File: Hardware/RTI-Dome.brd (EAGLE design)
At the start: 80 x 71.1 mm, 43 parts, among them IC1 24AA128ST, IC2 74LVC244, IC3 FT232RL, X13 PN61729-S

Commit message: Remove I2C 2 pin header as we now have the eeprom on the board.
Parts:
- removed JP4: (no value), jumper:JP1
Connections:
- net SCL: no longer JP4.1
- net SDA: no longer JP4.2
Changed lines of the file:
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@@
 <element name="C1" library="rti" package="C0805" value="10uF" x="30.734" y="54.61" rot="R90"/>
 <element name="R5" library="rti" package="R0805" value="100" x="33.02" y="54.61" rot="R90"/>
-<element name="JP4" library="jumper" package="JP1" value="" x="9.271" y="54.356" rot="R270"/>
 <element name="U$4" library="rti" package="LOGO_BIG" value="RTI-LOGO_BIG" x="3.175" y="18.542"/>
 <element name="C2" library="rti" package="UD-10X10_NICHICON" value="100uF" x="64.77" y="13.97" rot="R270"/>
@@
 </signal>
 <signal name="SDA">
-<contactref element="JP4" pad="2"/>
-<wire x1="10.541" y1="59.3725" x2="10.541" y2="54.356" width="0.4064" layer="1"/>
 <contactref element="PCB1" pad="SDA1"/>
 <contactref element="IC1" pad="5"/>
 <contactref element="R1" pad="1"/>
-<wire x1="10.541" y1="54.356" x2="10.541" y2="51.181" width="0.3048" layer="1"/>
 <wire x1="10.541" y1="51.181" x2="10.16" y2="50.8" width="0.3048" layer="1"/>
 <wire x1="6.055" y1="44.835" x2="6.055" y2="50.505" width="0.3048" layer="1"/>
@@
 <wire x1="7.96925" y1="44.13" x2="7.26425" y2="44.835" width="0.3048" layer="1"/>
 <wire x1="7.26425" y1="44.835" x2="6.055" y2="44.835" width="0.3048" layer="1"/>
+<wire x1="10.541" y1="59.3725" x2="10.541" y2="51.181" width="0.254" layer="1"/>
 </signal>
 <signal name="3.3V">
@@
 <contactref element="IC1" pad="6"/>
 <contactref element="R3" pad="1"/>
-<contactref element="JP4" pad="1"/>
-<wire x1="8.001" y1="59.3725" x2="8.001" y2="54.356" width="0.4064" layer="1"/>
 <contactref element="PCB1" pad="SCL1"/>
 <wire x1="5.405" y1="44.835" x2="5.405" y2="46.101" width="0.3048" layer="1"/>
@@
 <wire x1="6.35" y1="52.07" x2="7.62" y2="52.07" width="0.3048" layer="1"/>
 <wire x1="7.62" y1="52.07" x2="8.001" y2="52.451" width="0.3048" layer="1"/>
-<wire x1="8.001" y1="52.451" x2="8.001" y2="54.356" width="0.3048" layer="1"/>
 <wire x1="2.3495" y1="44.35225" x2="2.54" y2="44.54275" width="0.3048" layer="1"/>
 <wire x1="2.54" y1="44.54275" x2="2.54" y2="45.72" width="0.3048" layer="1"/>
 <wire x1="2.54" y1="45.72" x2="2.921" y2="46.101" width="0.3048" layer="1"/>
 <wire x1="2.921" y1="46.101" x2="5.405" y2="46.101" width="0.3048" layer="1"/>
+<wire x1="8.001" y1="59.3725" x2="8.001" y2="52.451" width="0.254" layer="1"/>
 </signal>
 <signal name="N$1">

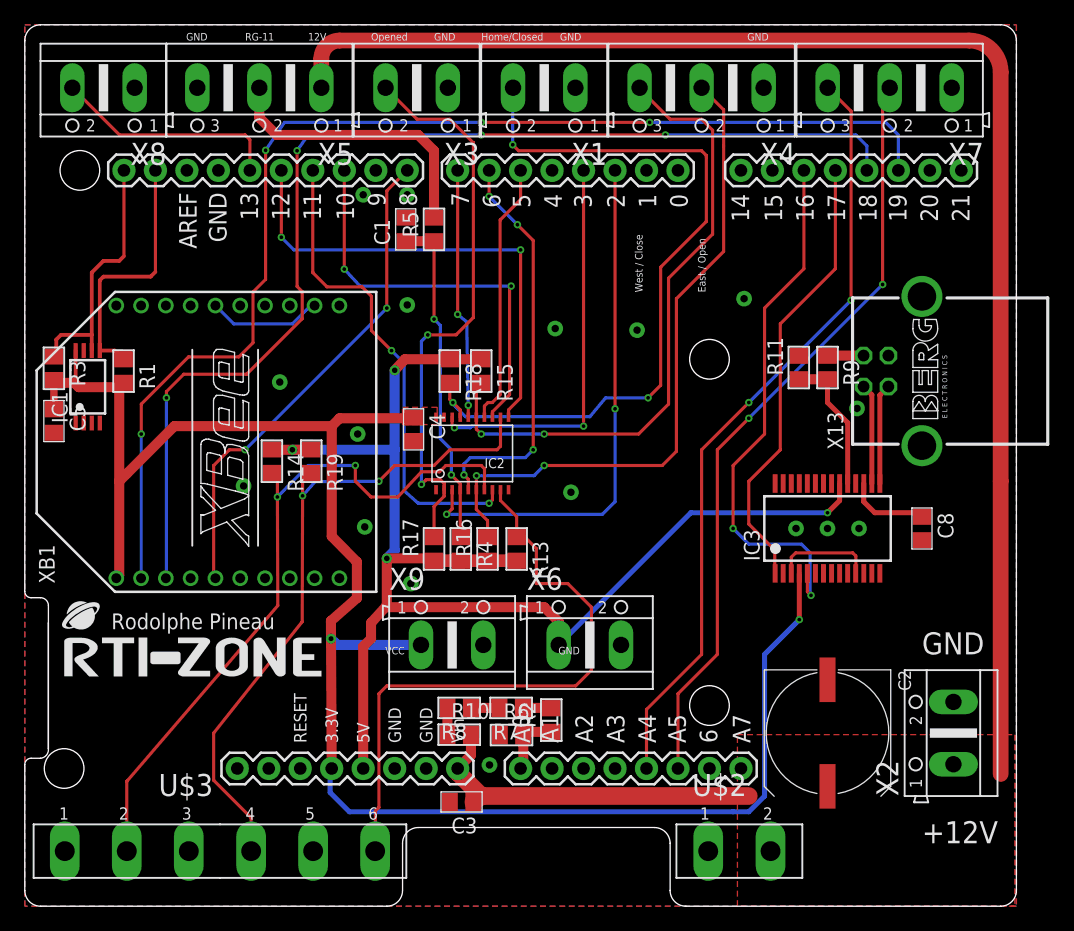
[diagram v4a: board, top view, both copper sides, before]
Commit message: Only focus on doing one board with terminal header. Removed the old one with STL connectors.
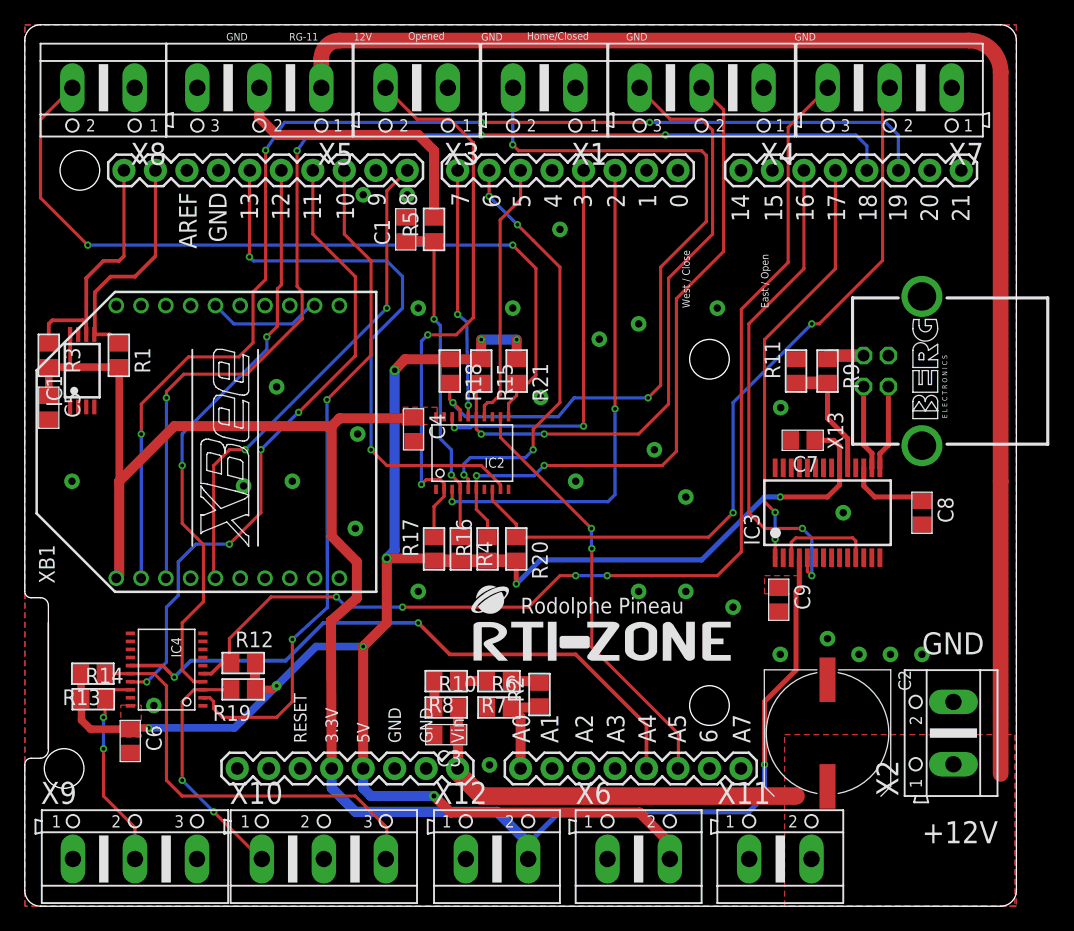
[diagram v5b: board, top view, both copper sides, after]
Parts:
- removed U$2: STL-140-2, rti:STL-140-2
- removed U$3: STL-140-6, rti:STL-140-6
- added C6, C7, C9: 100nF, rti:C0805
- added IC4: 74ABT244, rti:TSSOP20
- added R12, R20: 1K, rti:R0805
- added R21: 4.7K, rti:R0805
- added X10: (no value), con-ptr500:AK500/3
- added X11, X12: (no value), con-ptr500:AK500/2
- X9: device con-ptr500:AK500/2 -> con-ptr500:AK500/3
- moved R13 35.6 mm to (5.49, 18.8), turned to 180 degrees
- moved U$4 33.0 mm to (36.2, 19.8)
- moved X9 30.9 mm to (8.89, 3.81)
- moved R14 24.0 mm to (5.52, 16.7), turned to 0 degrees
- moved R19 19.2 mm to (17.6, 17.5), turned to 180 degrees
- moved X6 17.7 mm to (49.5, 3.81)
- moved C3 5.57 mm to (34.0, 13.8)
- moved R6 2.44 mm to (38.3, 16.0)
- moved R10 2.43 mm to (34.0, 16.0)
- moved R8 2.40 mm to (34.0, 18.2)
- moved R7 2.37 mm to (38.3, 18.2)
- moved R2 2.27 mm to (41.5, 17.1)
- moved IC1 1.38 mm to (4.64, 43.2)
- moved R1 1.33 mm to (7.59, 44.5)
- moved C8 1.27 mm to (72.4, 31.8)
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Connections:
- removed net 13: PCB1.13, X8.2
- new net AT_PARK_PIN_EXT: IC2.P$8, R20.1, X7.2
- new net AT_PARK_PIN_LOOP_EXT: IC4.P$5, R12.1, X7.3
- new net D13: IC2.P$9, PCB1.13
- new net D13_EXT: IC2.P$11, R21.2, X8.2
- net +12V: now also X11.2; no longer U$2.2
- net 3.3V: now also C9.1, X12.2; no longer X9.1
- net AT_PARK_PIN: now also IC2.P$12; no longer X7.2
- net AT_PARK_PIN_LOOP: now also IC4.P$15; no longer X7.3
- net GND: now also C6.2, C7.2, C9.2, IC4.P$1, IC4.P$10, IC4.P$19, X10.2, X11.1, X12.1, X6.1, X9.1, X9.3; no longer U$2.1, U$3.1, U$3.3, U$3.5, X6.2, X9.2
- net M_DIR: now also IC4.P$17; no longer IC2.P$8
- net M_DIR_5V: now also IC4.P$3, X10.1; no longer IC2.P$12, U$3.4
- net M_EN: now also IC4.P$2; no longer IC2.P$13
- net M_EN_5V: now also IC4.P$18, X9.2; no longer IC2.P$7, U$3.2
- net M_STEP: now also IC4.P$4; no longer IC2.P$11
- net M_STEP_5V: now also IC4.P$16, X10.3; no longer IC2.P$9, U$3.6
- net VCC: now also C6.1, C7.1, IC4.P$20, R12.2, R20.2, R21.1, X6.2; no longer X6.1
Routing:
- net AT_PARK_PIN_LOOP_EXT: track 0.00 -> 89.9 mm, vias 0 -> 4
- net D13_EXT: track 0.00 -> 65.7 mm, vias 0 -> 2
- net AT_PARK_PIN_EXT: track 0.00 -> 62.9 mm, vias 0 -> 2
- net VCC: track 107.7 -> 156.8 mm, vias 4 -> 10
- net D13: track 0.00 -> 47.0 mm, vias 0 -> 2
- net M_EN_5V: track 57.7 -> 16.4 mm
- net M_DIR_5V: track 54.5 -> 19.8 mm
- net AT_PARK_PIN: track 62.0 -> 34.3 mm
- net M_EN: track 33.2 -> 55.2 mm
- net 13: track 18.5 -> 0.00 mm
- net M_STEP_5V: track 50.2 -> 34.9 mm
- net M_DIR: track 39.0 -> 52.6 mm, vias 2 -> 4
- net AT_PARK_PIN_LOOP: track 62.5 -> 50.8 mm
- net M_STEP: track 39.0 -> 47.1 mm
- net +12V: track 144.0 -> 148.8 mm
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- added copper zone on layer 1, net VCC
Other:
- outline, holes or cut-outs redrawn
- board text removed: "VCC"

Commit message: All pull-up for external pinsare now 4.7K
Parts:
- R12, R13, R14, R19, R20: value 1K -> 4.7K
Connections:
- net GND: now also IC2.P$13, IC4.P$11, IC4.P$13, IC4.P$6, IC4.P$8
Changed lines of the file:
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@@
 <element name="C2" library="rti" package="UD-10X10_NICHICON" value="100uF" x="64.77" y="13.97" rot="R270"/>
 <element name="IC2" library="rti" package="TSSOP20" value="74LVC244" x="36.068" y="36.576" rot="R90"/>
-<element name="R13" library="rti" package="R0805" value="1K" x="5.49275" y="18.76425" rot="R180"/>
-<element name="R14" library="rti" package="R0805" value="1K" x="5.5245" y="16.7005"/>
+<element name="R13" library="rti" package="R0805" value="4.7K" x="5.49275" y="18.76425" rot="R180"/>
+<element name="R14" library="rti" package="R0805" value="4.7K" x="5.5245" y="16.7005"/>
 <element name="R15" library="rti" package="R0805" value="4.7K" x="36.83" y="43.18" rot="R270"/>
 <element name="R16" library="rti" package="R0805" value="4.7K" x="37.338" y="28.829" rot="R90"/>
 <element name="R17" library="rti" package="R0805" value="4.7K" x="33.02" y="28.829" rot="R90"/>
 <element name="R18" library="rti" package="R0805" value="4.7K" x="34.29" y="43.18" rot="R270"/>
-<element name="R19" library="rti" package="R0805" value="1K" x="17.62125" y="17.49425" rot="R180"/>
+<element name="R19" library="rti" package="R0805" value="4.7K" x="17.62125" y="17.49425" rot="R180"/>
 <element name="R6" library="rti" package="R0805" value="100K 0.1%" x="38.25875" y="16.03375"/>
 <element name="R7" library="rti" package="R0805" value="100K 0.1%" x="38.25875" y="18.161" rot="R180"/>
@@
 <element name="IC4" library="rti" package="TSSOP20" value="74ABT244" x="11.43" y="19.05" rot="R180"/>
 <element name="C6" library="rti" package="C0805" value="100nF" x="8.509" y="13.335" rot="R270"/>
-<element name="R12" library="rti" package="R0805" value="1K" x="17.62125" y="19.6215"/>
-<element name="R20" library="rti" package="R0805" value="1K" x="39.65575" y="28.829" rot="R270"/>
+<element name="R12" library="rti" package="R0805" value="4.7K" x="17.62125" y="19.6215"/>
+<element name="R20" library="rti" package="R0805" value="4.7K" x="39.65575" y="28.829" rot="R270"/>
 <element name="C7" library="rti" package="C0805" value="100nF" x="62.76975" y="37.592" rot="R180"/>
 <element name="C9" library="rti" package="C0805" value="100nF" x="60.833" y="24.73325" rot="R270"/>
@@
 <contactref element="X6" pad="1"/>
 <via x="66.04" y="31.75" extent="1-16" drill="0.6" diameter="1.27"/>
+<contactref element="IC2" pad="P$13"/>
+<contactref element="IC4" pad="P$6"/>
+<contactref element="IC4" pad="P$13"/>
+<contactref element="IC4" pad="P$8"/>
+<contactref element="IC4" pad="P$11"/>
 </signal>
 <signal name="+12V" class="1">

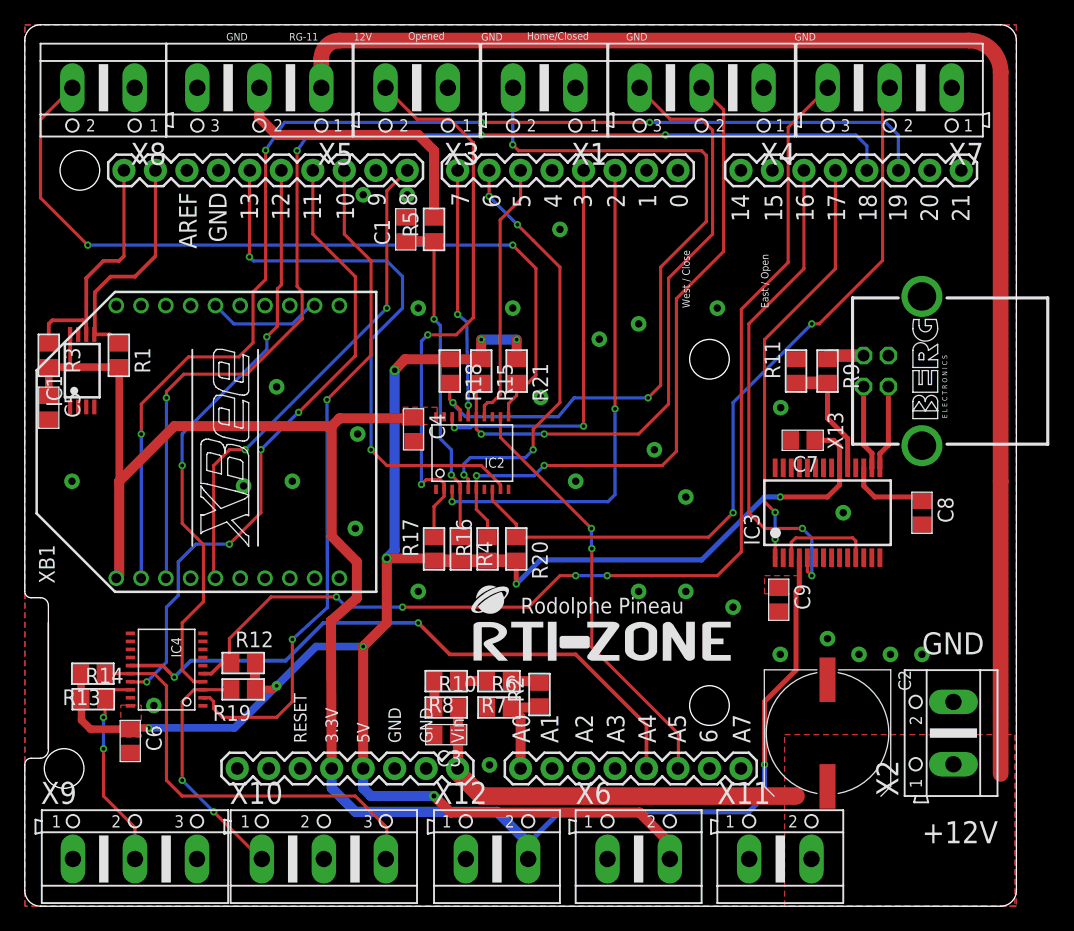
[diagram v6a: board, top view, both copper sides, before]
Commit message: Change the polarity on the en.dir,step pin to match the ISD0x too, so no more need to have some #define in the code
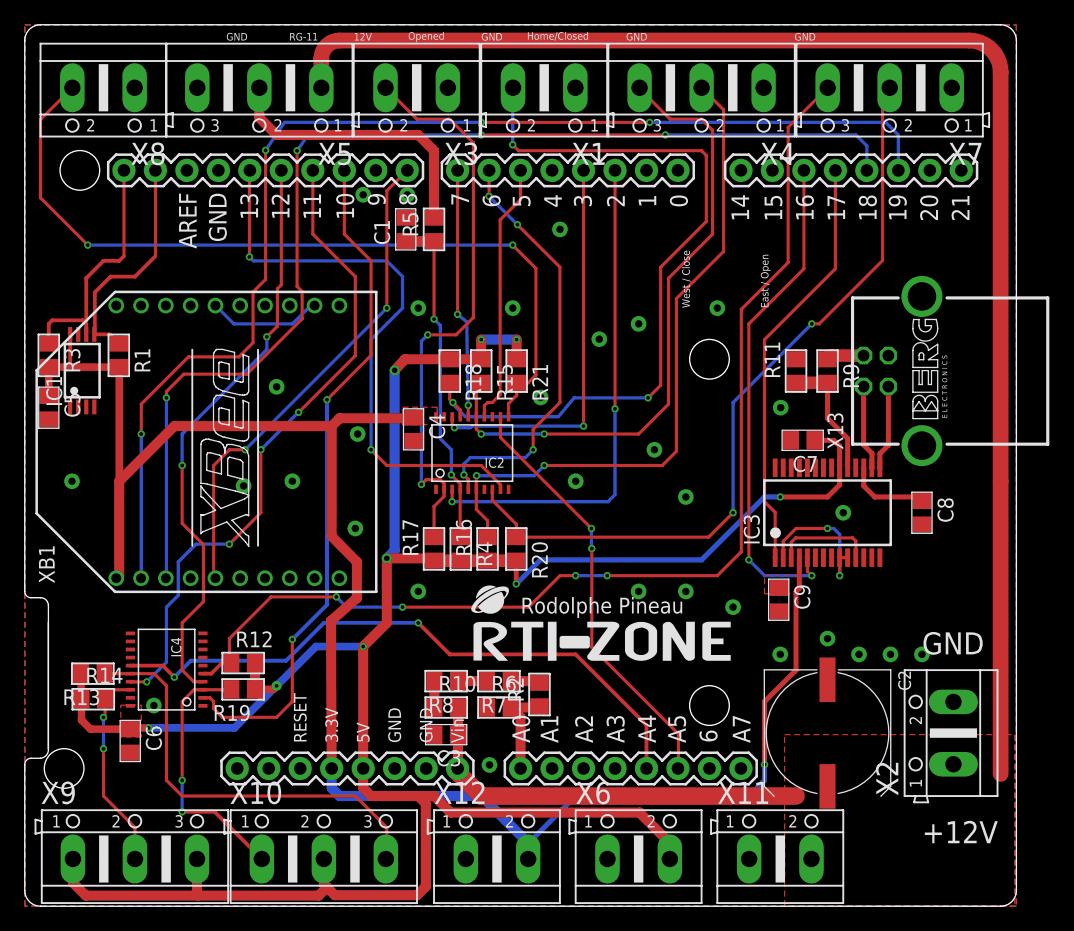
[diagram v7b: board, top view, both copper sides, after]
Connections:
- net N$4 renamed RTS_CTS
- removed net N$21: IC3.10
- new net DTR_DSR_DCD: IC3.10, IC3.2, IC3.9
- net GND: no longer X10.2, X9.1, X9.3
- net VCC: now also X10.2, X9.1, X9.3
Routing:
- net VCC: track 156.8 -> 201.4 mm, vias 10 -> 9
- net DTR_DSR_DCD: track 0.00 -> 11.9 mm, vias 0 -> 2
- net M_DIR_5V: track 19.8 -> 21.3 mm
- net 3.3V: track 144.8 -> 144.1 mm
- net RX2: vias 2 -> 0
